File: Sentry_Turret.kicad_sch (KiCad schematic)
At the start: 28 parts, among them J1 XT30_Y1, J10 Conn_01x02, J11 24V_Agi2, J12 172298-1108, J13 24V_Fly1, J15 24V_Fly3, J17 24V_Fly2, J19 24V_Fly4, J2 172298-1116, J21 19V_Orin, J22 3.3V_Debug, J3 XT30_P1, J4 Conn_01x02, J5 XT30_P2, J6 Conn_01x02, J7 XT30_Y2, J8 Conn_01x02, J9 24V_Agi1

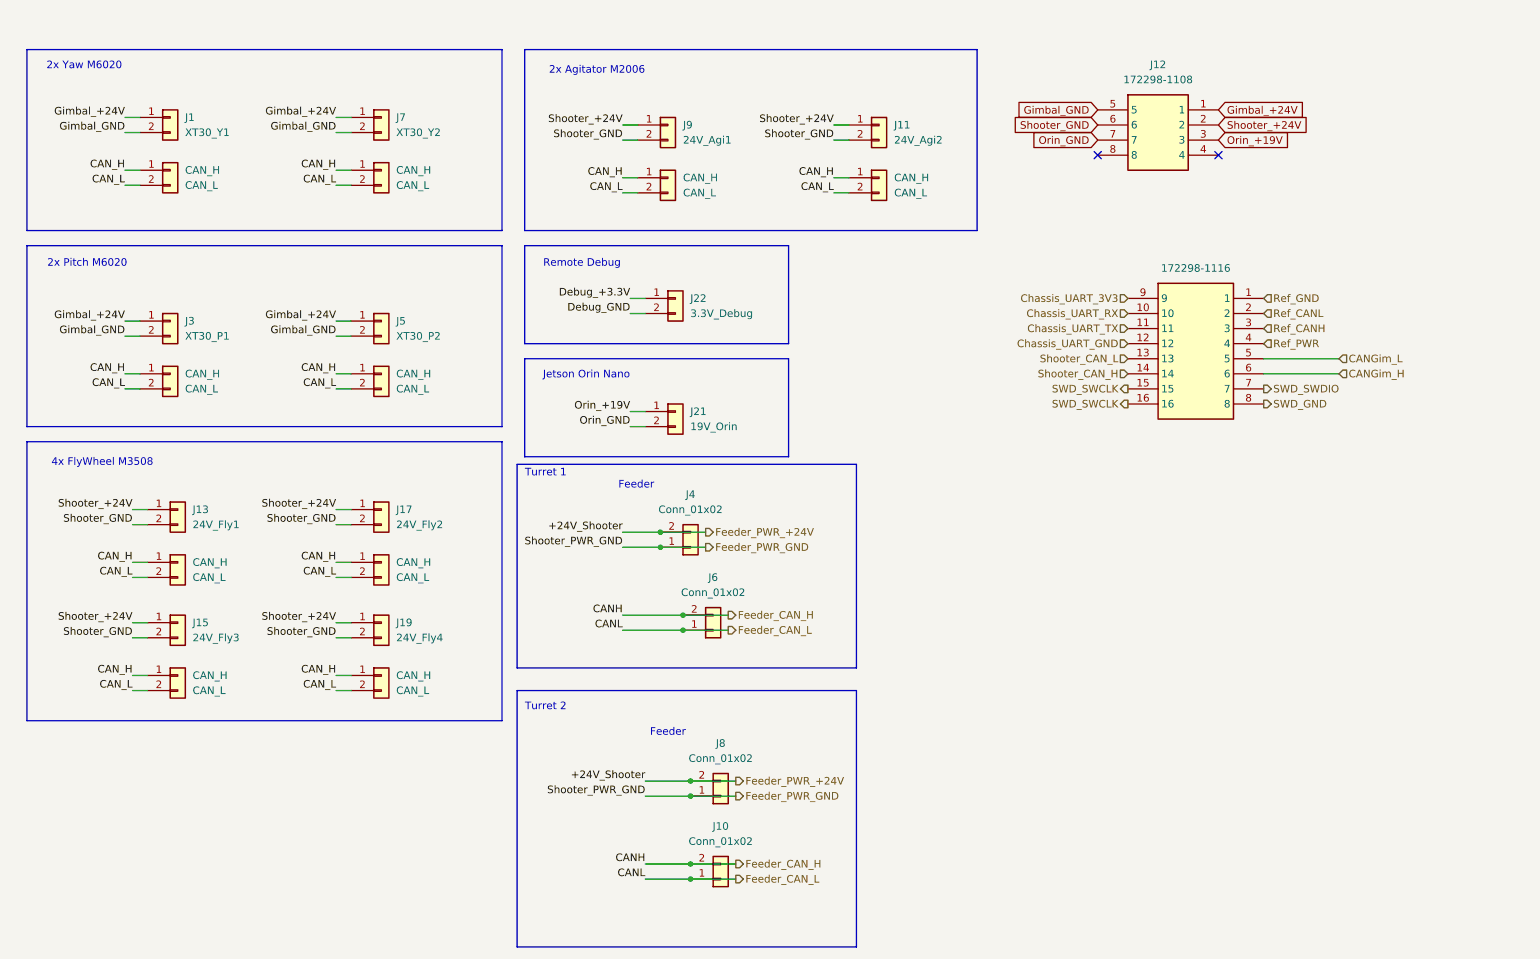
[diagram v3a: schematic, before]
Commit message: Swapped to copy of standard/hero sch
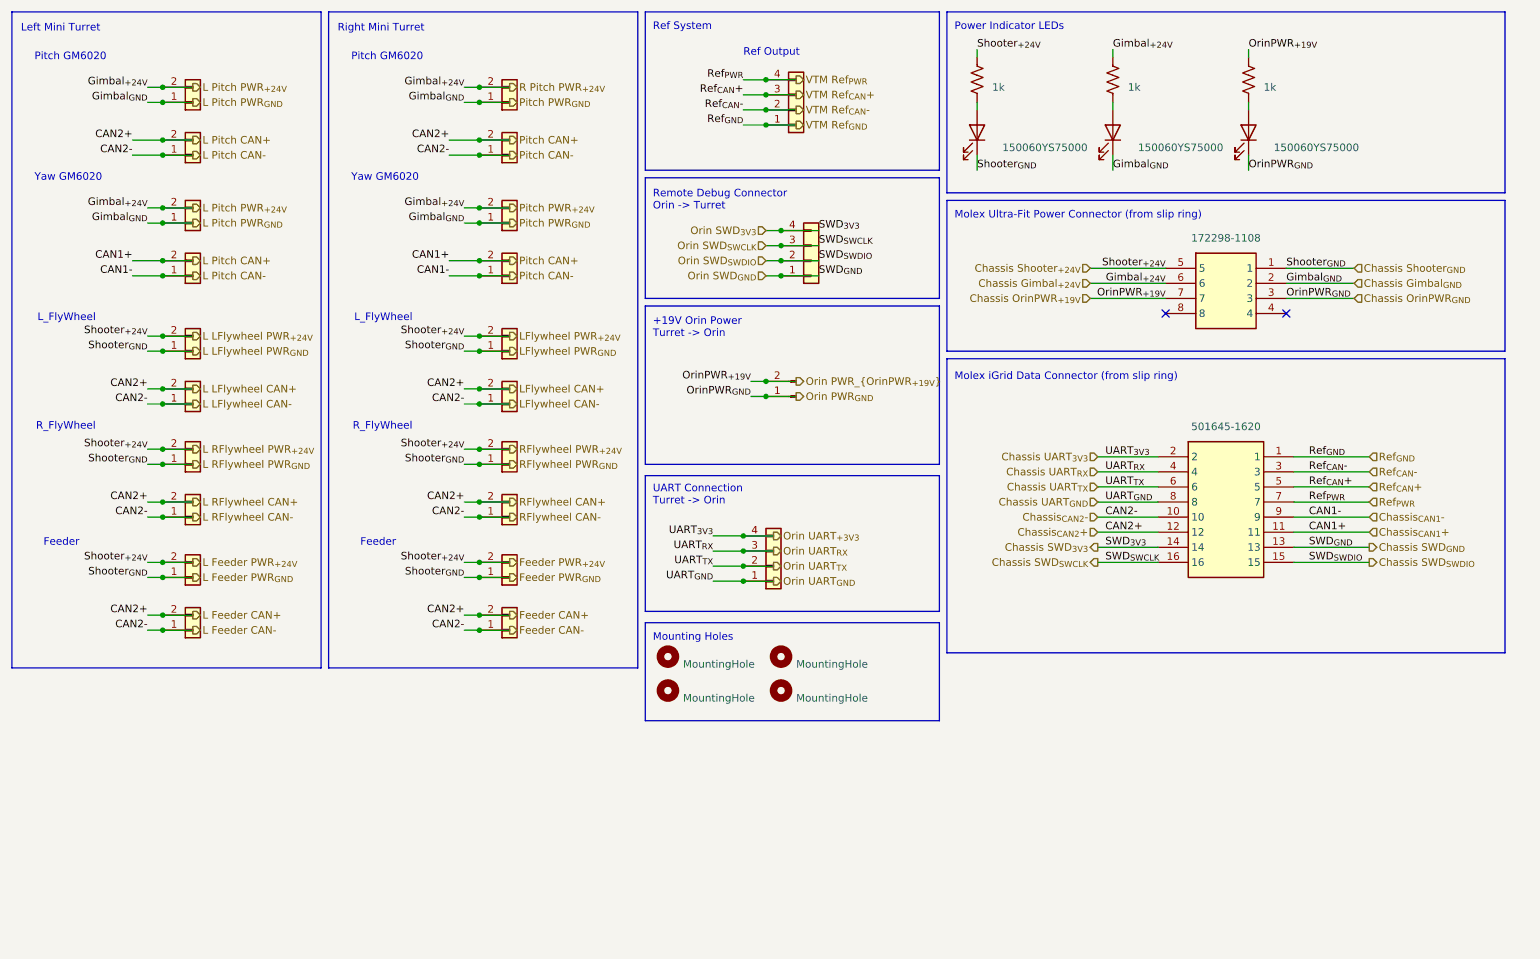
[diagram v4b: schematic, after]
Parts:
- removed CAN_H (x10): CAN_L, symbol Connector_Generic:Conn_01x02
- removed J1: XT30_Y1, symbol Connector_Generic:Conn_01x02
- removed J10, J4, J6, J8: Conn_01x02, symbol Connector_Generic:Conn_01x02
- removed J11: 24V_Agi2, symbol Connector_Generic:Conn_01x02
- removed J12: 172298-1108, 172298-YY08, symbol Robomaster:172298-1108
- removed J13: 24V_Fly1, symbol Connector_Generic:Conn_01x02
- removed J15: 24V_Fly3, symbol Connector_Generic:Conn_01x02
- removed J17: 24V_Fly2, symbol Connector_Generic:Conn_01x02
- removed J19: 24V_Fly4, symbol Connector_Generic:Conn_01x02
- removed J2: 172298-1116, 172298-YY16, symbol Robomaster_Library:172298-1116
- removed J21: 19V_Orin, symbol Connector_Generic:Conn_01x02
- removed J22: 3.3V_Debug, symbol Connector_Generic:Conn_01x02
- removed J3: XT30_P1, symbol Connector_Generic:Conn_01x02
- removed J5: XT30_P2, symbol Connector_Generic:Conn_01x02
- removed J7: XT30_Y2, symbol Connector_Generic:Conn_01x02
- removed J9: 24V_Agi1, symbol Connector_Generic:Conn_01x02
- added D1, D2, D3: 150060YS75000, LED_SMD:LED_0603_1608Metric_Pad1.05x0.95mm_HandSolder, symbol Device:LED
- added H1, H2, H3, H4: MountingHole, MountingHole:MountingHole_3mm, symbol Mechanical:MountingHole
- added J14: 501645-1620, 5016451620, symbol Robomaster_Library:501645-1620
- added J16: 172298-1108, 172298-YY08, symbol Robomaster_Library:172298-1108
- added L_+PWR_Agitator, L_PWR_LFly, L_PWR_Pitch, L_PWR_RFly, L_PWR_Yaw, R_PWR_Agitator, R_PWR_LFly, R_PWR_Pitch, R_PWR_RFly, R_PWR_Yaw: Conn_01x02_Pin, Connector_AMASS:AMASS_XT30U-F_1x02_P5.0mm_Vertical, symbol Connector_Generic:Conn_01x02
- added L_CAN_Agitator, L_CAN_LFly, L_CAN_Pitch, L_CAN_RFly, L_CAN_Yaw, R_CAN_LFly, R_CAN_Pitch, R_CAN_RFly, R_CAN_Yaw, R_PWR_Agitator: Conn_01x02_Pin, Connector_JST:JST_GH_BM02B-GHS-TBT_1x02-1MP_P1.25mm_Vertical, symbol Connector_Generic:Conn_01x02
- added PWR_Orin: Conn_01x02_Pin, Connector_AMASS:AMASS_XT30U-F_1x02_P5.0mm_Vertical, symbol Connector:Conn_01x02_Pin
- added R1, R2, R3: 1k, Resistor_SMD:R_0603_1608Metric_Pad0.98x0.95mm_HandSolder, symbol Device:R_US
- added Ref_Out1, SWD_In_Orin, UART_Orin: Conn_01x04_Pin, Connector_JST:JST_GH_BM04B-GHS-TBT_1x04-1MP_P1.25mm_Vertical, symbol Connector_Generic:Conn_01x04
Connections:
- new net: D1.2 (A), R1.2
- new net: D2.2 (A), R2.2
- new net: D3.2 (A), R3.2
- new net Chassis Gimbal_{+24V}: J16.6, L_PWR_Pitch.2 (Pin_2), L_PWR_Yaw.2 (Pin_2), R2.1, R_PWR_Pitch.2 (Pin_2), R_PWR_Yaw.2 (Pin_2)
- new net Chassis Gimbal_{GND}: D2.1 (K), J16.2, L_PWR_Pitch.1 (Pin_1), L_PWR_Yaw.1 (Pin_1), R_PWR_Pitch.1 (Pin_1), R_PWR_Yaw.1 (Pin_1)
- new net Chassis OrinPWR_{+19V}: J16.7, PWR_Orin.2 (Pin_2), R3.1
- new net Chassis OrinPWR_{GND}: D3.1 (K), J16.3, PWR_Orin.1 (Pin_1)
- new net Chassis SWD_{3V3}: J14.14, SWD_In_Orin.4 (Pin_4)
- new net Chassis SWD_{GND}: J14.13, SWD_In_Orin.1 (Pin_1)
- new net Chassis SWD_{SWCLK}: J14.16, SWD_In_Orin.3 (Pin_3)
- new net Chassis SWD_{SWDIO}: J14.15, SWD_In_Orin.2 (Pin_2)
- new net Chassis Shooter_{+24V}: J16.5, L_+PWR_Agitator.2 (Pin_2), L_PWR_LFly.2 (Pin_2), L_PWR_RFly.2 (Pin_2), R1.1, R_PWR_Agitator.2 (Pin_2), R_PWR_LFly.2 (Pin_2), R_PWR_RFly.2 (Pin_2)
- new net Chassis Shooter_{GND}: D1.1 (K), J16.1, L_+PWR_Agitator.1 (Pin_1), L_PWR_LFly.1 (Pin_1), L_PWR_RFly.1 (Pin_1), R_PWR_Agitator.1 (Pin_1), R_PWR_LFly.1 (Pin_1), R_PWR_RFly.1 (Pin_1)
- new net Chassis UART_{3V3}: J14.2, UART_Orin.4 (Pin_4)
- new net Chassis UART_{GND}: J14.8, UART_Orin.1 (Pin_1)
- new net Chassis UART_{RX}: J14.4, UART_Orin.3 (Pin_3)
- new net Chassis UART_{TX}: J14.6, UART_Orin.2 (Pin_2)
- new net Chassis_{CAN1}+: J14.11, J14.12, L_CAN_Agitator.2 (Pin_2), L_CAN_LFly.2 (Pin_2), L_CAN_Pitch.2 (Pin_2), L_CAN_RFly.2 (Pin_2), L_CAN_Yaw.2 (Pin_2), R_CAN_LFly.2 (Pin_2), R_CAN_Pitch.2 (Pin_2), R_CAN_RFly.2 (Pin_2), R_CAN_Yaw.2 (Pin_2), R_PWR_Agitator.2 (Pin_2)
- new net Chassis_{CAN1}-: J14.10, J14.9, L_CAN_Agitator.1 (Pin_1), L_CAN_LFly.1 (Pin_1), L_CAN_Pitch.1 (Pin_1), L_CAN_RFly.1 (Pin_1), L_CAN_Yaw.1 (Pin_1), R_CAN_LFly.1 (Pin_1), R_CAN_Pitch.1 (Pin_1), R_CAN_RFly.1 (Pin_1), R_CAN_Yaw.1 (Pin_1), R_PWR_Agitator.1 (Pin_1)
- new net Ref_{CAN}+: J14.5, Ref_Out1.3 (Pin_3)
- new net Ref_{CAN}-: J14.3, Ref_Out1.2 (Pin_2)
- new net Ref_{GND}: J14.1, Ref_Out1.1 (Pin_1)
- new net Ref_{PWR}: J14.7, Ref_Out1.4 (Pin_4)
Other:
- note added: "+19V Orin Power Turret -> Orin"
- note added: "L_FlyWheel"
- note added: "Left Mini Turret"
- note added: "Molex Ultra-Fit Power Connector (from slip ring)"
- note added: "Molex iGrid Data Connector (from slip ring)"
- note added: "Mounting Holes"
- note added: "Pitch GM6020"
- note added: "Power Indicator LEDs"
- note added: "R_FlyWheel"
- note added: "Ref Output"
- note added: "Ref System"
- note added: "Remote Debug Connector Orin -> Turret"
- note added: "Right Mini Turret"
- note added: "UART Connection Turret -> Orin"
- note added: "Yaw GM6020"
- note removed: "2x Agitator M2006"
- note removed: "2x Pitch M6020"
- note removed: "2x Yaw M6020"
- note removed: "4x FlyWheel M3508"
- note removed: "Jetson Orin Nano"
- note removed: "Remote Debug"
- note removed: "Turret 1"
- note removed: "Turret 2"
